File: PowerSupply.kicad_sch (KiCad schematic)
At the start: 50 parts, among them Q1 CSD17318Q2, Q2 CSD17318Q2, U1 TPS55288RPMR

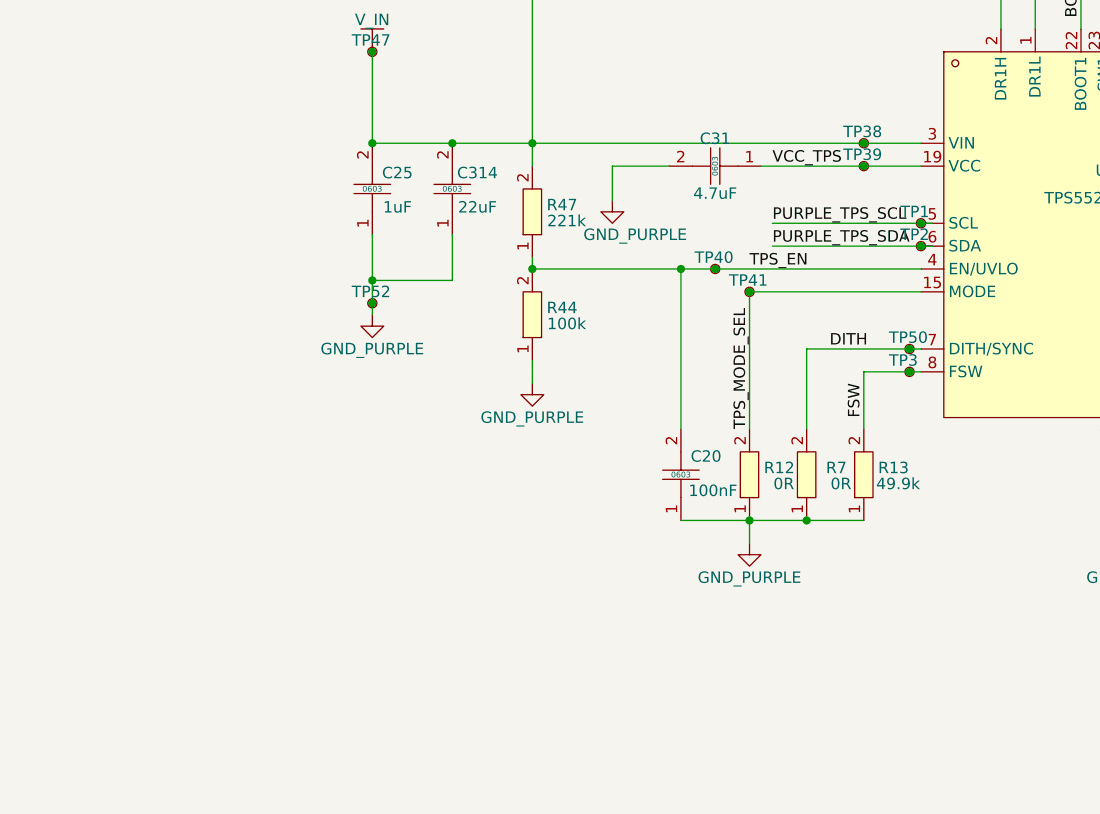
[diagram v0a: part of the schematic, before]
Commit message: Adding Quicc connector
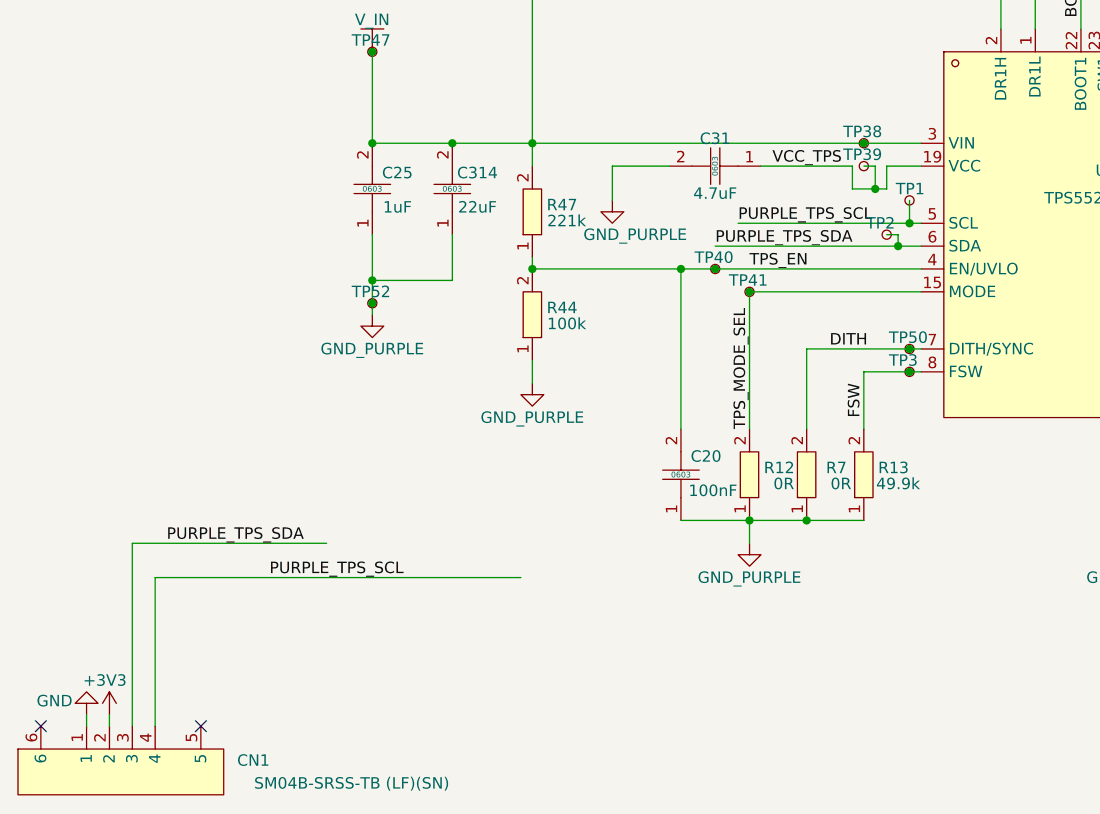
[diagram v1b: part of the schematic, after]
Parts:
- added CN1: SM04B-SRSS-TB (LF)(SN), easyeda2kicad:CONN-SMD_4P-P1.00_SM04B-SRSS-TB-LF-SN, symbol easyeda2kicad:SM04B-SRSS-TB(LF)(SN)
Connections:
- net PURPLE_TPS_SCL: now also CN1.4
- net PURPLE_TPS_SDA: now also CN1.3
- new net +3V3: CN1.2
- new net GND: CN1.1
- no-connect marks 0 -> 2

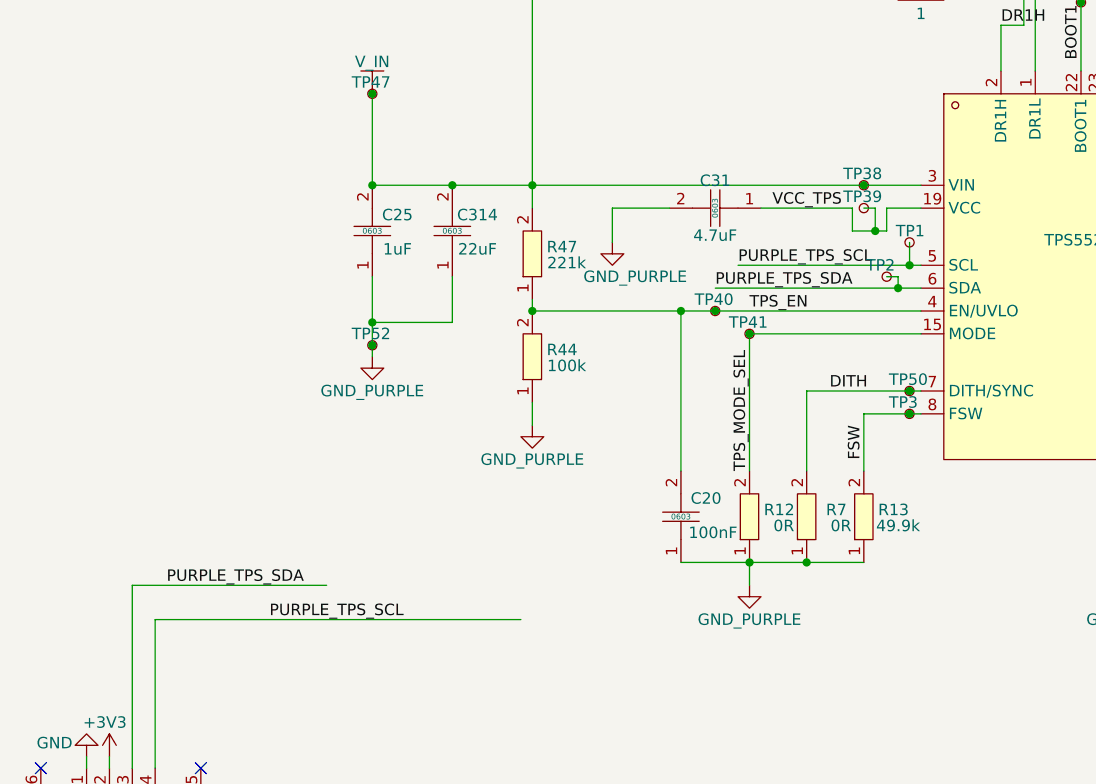
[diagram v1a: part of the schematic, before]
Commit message: Recreate TPS block in KiCad with 0603+ components
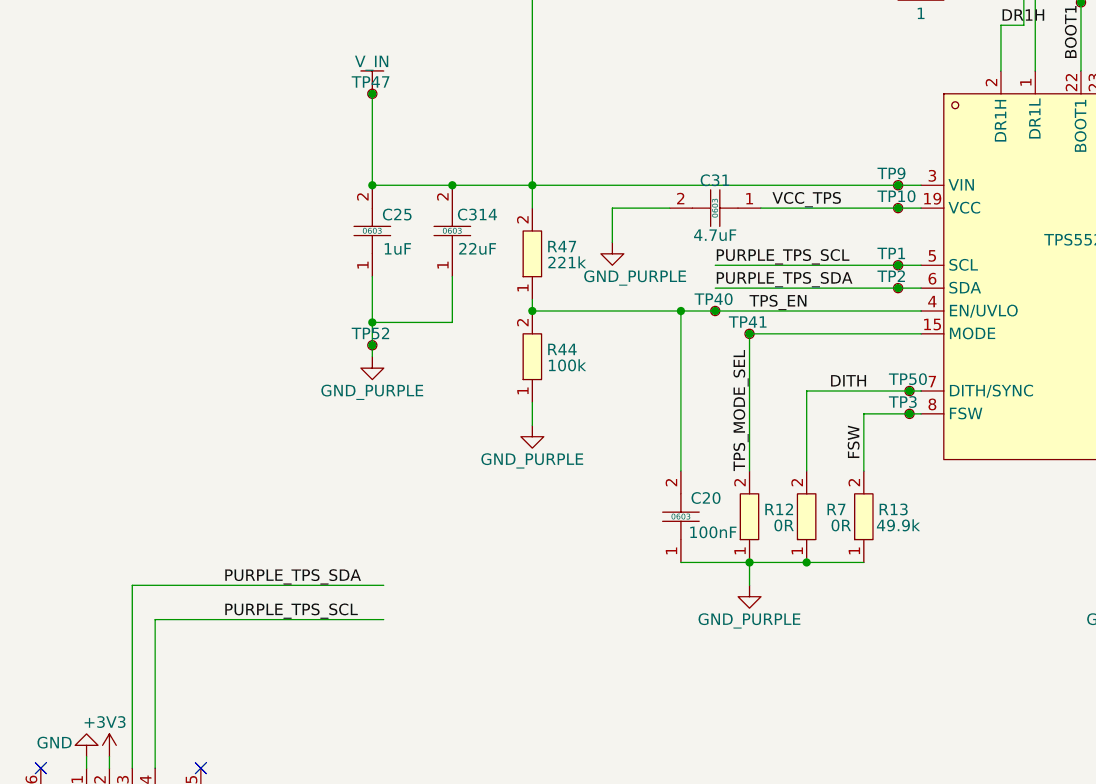
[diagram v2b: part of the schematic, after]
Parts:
- removed TP38, TP39: TestPoint_Small, symbol Connector:TestPoint_Small
- added TP10, TP9: TestPoint_Small, symbol Connector:TestPoint_Small
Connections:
- net VCC_TPS: now also TP10.1
- net at C25.2, C314.2, Q1.1 (D)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: now also TP9.1
